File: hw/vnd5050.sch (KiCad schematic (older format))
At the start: 8 parts, among them U301 VND5050AJTR-E

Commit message: 050518: Kikepera head prototype first revision, saw not working
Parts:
- C301: symbol 4.7uF -> icu-rescue:4.7uF
- D301, D302, D303: symbol DIODE_RS07J-GS18 -> icu-rescue:DIODE_RS07J-GS18
- R301, R302: symbol 1K -> icu-rescue:1K
- R303: symbol 390 -> icu-rescue:390
- U301: symbol VND5050AJTR-E -> icu-rescue:VND5050AJTR-E
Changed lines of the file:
@@
-EESchema Schematic File Version 2
-LIBS:kemet
-LIBS:usevolt
-LIBS:wurth_elektronik_LED
-LIBS:power
-LIBS:yageo
+EESchema Schematic File Version 4
 LIBS:icu-cache
 EELAYER 26 0
@@
 SENSE
 $Comp
-L VND5050AJTR-E U301
+L icu-rescue:VND5050AJTR-E U301
 U 1 1 59D8088A
 P 4600 4000
@@
 AR Path="/5A7B577E/59D8088A" Ref="U801"  Part="1"
 AR Path="/5A7B753D/59D8088A" Ref="U901"  Part="1"
-F 0 "U301" H 4700 4447 60  0000 C CNN
+F 0 "U501" H 4700 4447 60  0000 C CNN
 F 1 "VND5050AJTR-E" H 4700 4341 60  0000 C CNN
 F 2 "usevolt:PowerSSO-12" H 4600 4400 60  0001 C CNN
@@
 $EndComp
 $Comp
-L VDD #PWR045
+L icu-rescue:VDD #PWR045
 U 1 1 59D808C7
 P 5250 3650
@@
 AR Path="/5A7B577E/59D808C7" Ref="#PWR029"  Part="1"
 AR Path="/5A7B753D/59D808C7" Ref="#PWR033"  Part="1"
-F 0 "#PWR045" H 5250 3500 50  0001 C CNN
+F 0 "#PWR017" H 5250 3500 50  0001 C CNN
 F 1 "VDD" H 5267 3823 50  0000 C CNN
 F 2 "" H 5250 3650 50  0000 C CNN
@@
 $EndComp
 $Comp
-L GND #PWR046
+L icu-rescue:GND #PWR046
 U 1 1 59D86DC2
 P 2950 4450
@@
 AR Path="/5A7B577E/59D86DC2" Ref="#PWR030"  Part="1"
 AR Path="/5A7B753D/59D86DC2" Ref="#PWR034"  Part="1"
-F 0 "#PWR046" H 2950 4200 50  0001 C CNN
+F 0 "#PWR018" H 2950 4200 50  0001 C CNN
 F 1 "GND" H 2955 4277 50  0000 C CNN
 F 2 "" H 2950 4450 50  0000 C CNN
@@
 $EndComp
 $Comp
-L 390 R?
+L icu-rescue:390 R?
 U 1 1 59D88845
 P 3150 3550
@@
 AR Path="/5A7B577E/59D88845" Ref="R803"  Part="1"
 AR Path="/5A7B753D/59D88845" Ref="R903"  Part="1"
-F 0 "R303" H 3200 3734 45  0000 C CNN
+F 0 "R503" H 3200 3734 45  0000 C CNN
 F 1 "390" H 3200 3650 45  0000 C CNN
 F 2 "yageo:0603" H 3180 3700 20  0001 C CNN
@@
 $EndComp
 $Comp
-L 1K R?
+L icu-rescue:1K R?
 U 1 1 5A05950C
 P 2750 3550
@@
 AR Path="/5A7B577E/5A05950C" Ref="R801"  Part="1"
 AR Path="/5A7B753D/5A05950C" Ref="R901"  Part="1"
-F 0 "R301" H 2800 3734 45  0000 C CNN
+F 0 "R501" H 2800 3734 45  0000 C CNN
 F 1 "1K" H 2800 3650 45  0000 C CNN
 F 2 "yageo:0603" H 2780 3700 20  0001 C CNN
@@
 $EndComp
 $Comp
-L 1K R?
+L icu-rescue:1K R?
 U 1 1 5A059568
 P 2750 4100
@@
 AR Path="/5A7B577E/5A059568" Ref="R802"  Part="1"
 AR Path="/5A7B753D/5A059568" Ref="R902"  Part="1"
-F 0 "R302" H 2800 4284 45  0000 C CNN
+F 0 "R502" H 2800 4284 45  0000 C CNN
 F 1 "1K" H 2800 4200 45  0000 C CNN
 F 2 "yageo:0603" H 2780 4250 20  0001 C CNN
@@
 $EndComp
 $Comp
-L DIODE_RS07J-GS18 D302
+L icu-rescue:DIODE_RS07J-GS18 D302
 U 1 1 5A2AAF9E
 P 5450 4750
@@
 AR Path="/5A7B577E/5A2AAF9E" Ref="D802"  Part="1"
 AR Path="/5A7B753D/5A2AAF9E" Ref="D902"  Part="1"
-F 0 "D302" V 5400 4652 45  0000 R CNN
+F 0 "D502" V 5400 4652 45  0000 R CNN
 F 1 "DIODE_RS07J-GS18" H 5470 4690 45  0001 L BNN
 F 2 "usevolt:DO219AB" H 5480 4900 20  0001 C CNN
@@
 $EndComp
 $Comp
-L DIODE_RS07J-GS18 D303
+L icu-rescue:DIODE_RS07J-GS18 D303
 U 1 1 5A2AB087
 P 5700 4750
@@
 AR Path="/5A7B577E/5A2AB087" Ref="D803"  Part="1"
 AR Path="/5A7B753D/5A2AB087" Ref="D903"  Part="1"
-F 0 "D303" V 5650 4652 45  0000 R CNN
+F 0 "D503" V 5650 4652 45  0000 R CNN
 F 1 "DIODE_RS07J-GS18" H 5720 4690 45  0001 L BNN
 F 2 "usevolt:DO219AB" H 5730 4900 20  0001 C CNN
@@
 $EndComp
 $Comp
-L GND #PWR047
+L icu-rescue:GND #PWR047
 U 1 1 5A2AB10F
 P 5550 5150
@@
 AR Path="/5A7B577E/5A2AB10F" Ref="#PWR031"  Part="1"
 AR Path="/5A7B753D/5A2AB10F" Ref="#PWR035"  Part="1"
-F 0 "#PWR047" H 5550 4900 50  0001 C CNN
+F 0 "#PWR019" H 5550 4900 50  0001 C CNN
 F 1 "GND" H 5555 4977 50  0000 C CNN
 F 2 "" H 5550 5150 50  0000 C CNN
@@
 $EndComp
 Wire Wire Line
-	5250 3650 5250 4000
+	5250 3650 5250 3800
 Wire Wire Line
 	5250 3800 5100 3800
@@
 Connection ~ 5250 3900
 Wire Wire Line
-	5100 4100 5800 4100
+	5100 4100 5250 4100
 Wire Wire Line
 	5100 4200 5250 4200
@@
 Connection ~ 5250 4100
 Wire Wire Line
-	5100 4400 5800 4400
+	5100 4400 5250 4400
 Wire Wire Line
 	5100 4300 5250 4300
@@
 Connection ~ 5250 4400
 Wire Wire Line
-	2550 3450 4300 3450
-Wire Wire Line
-	2550 4000 4300 4000
-Wire Wire Line
-	2950 3550 2950 4450
+	2550 3450 2650 3450
+Wire Wire Line
+	2550 4000 2650 4000
+Wire Wire Line
+	2950 3550 2950 4100
 Wire Wire Line
 	2950 4300 4300 4300
@@
 Connection ~ 2950 4100
 Wire Wire Line
-	3350 3550 4150 3550
-Wire Wire Line
-	3500 3200 3500 3550
+	3350 3550 3500 3550
+Wire Wire Line
+	3500 3200 3500 3350
 Wire Wire Line
 	3500 3350 2550 3350
@@
 	5700 5050 5700 4950
 Wire Wire Line
-	5450 5050 5700 5050
+	5450 5050 5550 5050
 Wire Wire Line
 	5450 5050 5450 4950
@@
 	4300 3900 4150 3900
 Wire Wire Line
-	4150 3550 4150 4100
+	4150 3550 4150 3900
 Wire Wire Line
 	4300 3450 4300 3800
 $Comp
-L 4.7uF C301
+L icu-rescue:4.7uF C301
 U 1 1 5A708309
 P 3150 3850
@@
 AR Path="/5A7B577E/5A708309" Ref="C801"  Part="1"
 AR Path="/5A7B753D/5A708309" Ref="C901"  Part="1"
-F 0 "C301" H 3200 4049 45  0000 C CNN
+F 0 "C501" H 3200 4049 45  0000 C CNN
 F 1 "4.7uF" H 3200 3965 45  0000 C CNN
 F 2 "kemet:0603" H 3180 4000 20  0001 C CNN
@@
 Connection ~ 4150 3900
 $Comp
-L DIODE_RS07J-GS18 D301
+L icu-rescue:DIODE_RS07J-GS18 D301
 U 1 1 5A7BC689
 P 3700 3200
@@
 AR Path="/5A7B577E/5A7BC689" Ref="D801"  Part="1"
 AR Path="/5A7B753D/5A7BC689" Ref="D901"  Part="1"
-F 0 "D301" H 3650 3340 45  0000 C CNN
+F 0 "D501" H 3650 3340 45  0000 C CNN
 F 1 "DIODE_RS07J-GS18" H 3720 3140 45  0001 L BNN
 F 2 "usevolt:DO219AB" H 3730 3350 20  0001 C CNN
@@
 Connection ~ 3500 3350
 $Comp
-L +3V3 #PWR048
+L icu-rescue:+3V3 #PWR048
 U 1 1 5A7BC750
 P 3900 3100
@@
 AR Path="/5A7B577E/5A7BC750" Ref="#PWR032"  Part="1"
 AR Path="/5A7B753D/5A7BC750" Ref="#PWR036"  Part="1"
-F 0 "#PWR048" H 3900 2950 50  0001 C CNN
+AR Path="/5A7BC750" Ref="#PWR048"  Part="1"
+F 0 "#PWR020" H 3900 2950 50  0001 C CNN
 F 1 "+3V3" H 3915 3273 50  0000 C CNN
 F 2 "" H 3900 3100 50  0000 C CNN
@@
 Wire Wire Line
 	3900 3200 3800 3200
+Wire Wire Line
+	5250 3800 5250 3900
+Wire Wire Line
+	5250 3900 5250 4000
+Wire Wire Line
+	5250 4100 5450 4100
+Wire Wire Line
+	5250 4400 5700 4400
+Wire Wire Line
+	2950 4300 2950 4450
+Wire Wire Line
+	2950 4100 2950 4300
+Wire Wire Line
+	3500 3550 4150 3550
+Wire Wire Line
+	2650 3450 4300 3450
+Wire Wire Line
+	2650 4000 4300 4000
+Wire Wire Line
+	5700 4400 5800 4400
+Wire Wire Line
+	5450 4100 5800 4100
+Wire Wire Line
+	5550 5050 5700 5050
+Wire Wire Line
+	4150 3900 4150 4100
+Wire Wire Line
+	3500 3350 3500 3550
 $EndSCHEMATC

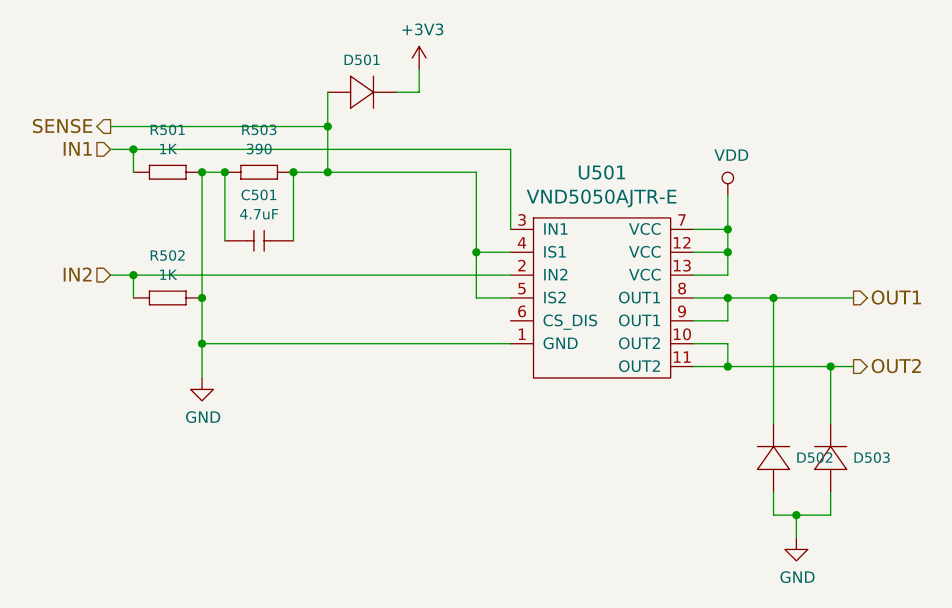
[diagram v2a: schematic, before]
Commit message: analog inputs replaced with digital inputs
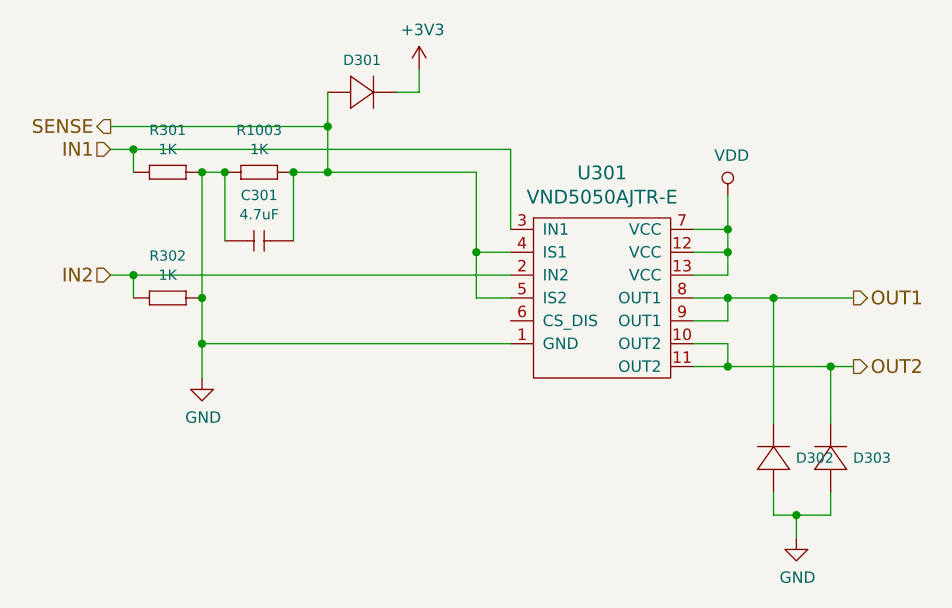
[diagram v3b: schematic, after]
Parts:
- removed R303: 390, yageo:0603, symbol icu-rescue:390
- added R603: 1K, yageo:0603, symbol yageo:1K
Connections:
- net GND: now also R603.2 (R2)
- net SENSE: now also R603.1 (R1)
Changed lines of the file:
@@
 $Descr A4 11693 8268
 encoding utf-8
-Sheet 4 14
+Sheet 6 10
 Title ""
 Date ""
@@
 AR Path="/5A7B577E/59D8088A" Ref="U801"  Part="1"
 AR Path="/5A7B753D/59D8088A" Ref="U901"  Part="1"
-F 0 "U501" H 4700 4447 60  0000 C CNN
+F 0 "U301" H 4700 4447 60  0000 C CNN
 F 1 "VND5050AJTR-E" H 4700 4341 60  0000 C CNN
 F 2 "usevolt:PowerSSO-12" H 4600 4400 60  0001 C CNN
@@
 AR Path="/5A7B577E/59D808C7" Ref="#PWR029"  Part="1"
 AR Path="/5A7B753D/59D808C7" Ref="#PWR033"  Part="1"
-F 0 "#PWR017" H 5250 3500 50  0001 C CNN
+F 0 "#PWR045" H 5250 3500 50  0001 C CNN
 F 1 "VDD" H 5267 3823 50  0000 C CNN
 F 2 "" H 5250 3650 50  0000 C CNN
@@
 AR Path="/5A7B577E/59D86DC2" Ref="#PWR030"  Part="1"
 AR Path="/5A7B753D/59D86DC2" Ref="#PWR034"  Part="1"
-F 0 "#PWR018" H 2950 4200 50  0001 C CNN
+F 0 "#PWR046" H 2950 4200 50  0001 C CNN
 F 1 "GND" H 2955 4277 50  0000 C CNN
 F 2 "" H 2950 4450 50  0000 C CNN
 F 3 "" H 2950 4450 50  0000 C CNN
 	1    2950 4450
-	1    0    0    -1
-$EndComp
-$Comp
-L icu-rescue:390 R?
-U 1 1 59D88845
-P 3150 3550
-AR Path="/5A015FC0/59D88845" Ref="R?"  Part="1"
-AR Path="/5A02A41F/59D88845" Ref="R?"  Part="1"
-AR Path="/5A12B58E/59D88845" Ref="R?"  Part="1"
-AR Path="/5A7B157A/59D88845" Ref="R303"  Part="1"
-AR Path="/5A7B341B/59D88845" Ref="R503"  Part="1"
-AR Path="/5A7B2C1B/59D88845" Ref="R403"  Part="1"
-AR Path="/5A7B3FAD/59D88845" Ref="R603"  Part="1"
-AR Path="/5A7B4C13/59D88845" Ref="R703"  Part="1"
-AR Path="/5A7B577E/59D88845" Ref="R803"  Part="1"
-AR Path="/5A7B753D/59D88845" Ref="R903"  Part="1"
-F 0 "R503" H 3200 3734 45  0000 C CNN
-F 1 "390" H 3200 3650 45  0000 C CNN
-F 2 "yageo:0603" H 3180 3700 20  0001 C CNN
-F 3 "" H 3119 3589 60  0001 C CNN
-F 4 "" H 3519 3989 60  0001 C CNN "1st Source Part Number"
-F 5 "Digikey" H 3419 3889 60  0001 C CNN "1st Source"
-F 6 "RC0603FR-07390RL" H 3319 3789 60  0001 C CNN "Manufacturer Part Number"
-F 7 "YAGEO" H 3219 3689 60  0001 C CNN "Manufacturer"
-	1    3150 3550
 	1    0    0    -1
 $EndComp
@@
 AR Path="/5A7B577E/5A05950C" Ref="R801"  Part="1"
 AR Path="/5A7B753D/5A05950C" Ref="R901"  Part="1"
-F 0 "R501" H 2800 3734 45  0000 C CNN
+F 0 "R301" H 2800 3734 45  0000 C CNN
 F 1 "1K" H 2800 3650 45  0000 C CNN
 F 2 "yageo:0603" H 2780 3700 20  0001 C CNN
@@
 AR Path="/5A7B577E/5A059568" Ref="R802"  Part="1"
 AR Path="/5A7B753D/5A059568" Ref="R902"  Part="1"
-F 0 "R502" H 2800 4284 45  0000 C CNN
+F 0 "R302" H 2800 4284 45  0000 C CNN
 F 1 "1K" H 2800 4200 45  0000 C CNN
 F 2 "yageo:0603" H 2780 4250 20  0001 C CNN
@@
 AR Path="/5A7B577E/5A2AAF9E" Ref="D802"  Part="1"
 AR Path="/5A7B753D/5A2AAF9E" Ref="D902"  Part="1"
-F 0 "D502" V 5400 4652 45  0000 R CNN
+F 0 "D302" V 5400 4652 45  0000 R CNN
 F 1 "DIODE_RS07J-GS18" H 5470 4690 45  0001 L BNN
 F 2 "usevolt:DO219AB" H 5480 4900 20  0001 C CNN
@@
 AR Path="/5A7B577E/5A2AB087" Ref="D803"  Part="1"
 AR Path="/5A7B753D/5A2AB087" Ref="D903"  Part="1"
-F 0 "D503" V 5650 4652 45  0000 R CNN
+F 0 "D303" V 5650 4652 45  0000 R CNN
 F 1 "DIODE_RS07J-GS18" H 5720 4690 45  0001 L BNN
 F 2 "usevolt:DO219AB" H 5730 4900 20  0001 C CNN
@@
 AR Path="/5A7B577E/5A2AB10F" Ref="#PWR031"  Part="1"
 AR Path="/5A7B753D/5A2AB10F" Ref="#PWR035"  Part="1"
-F 0 "#PWR019" H 5550 4900 50  0001 C CNN
+F 0 "#PWR047" H 5550 4900 50  0001 C CNN
 F 1 "GND" H 5555 4977 50  0000 C CNN
 F 2 "" H 5550 5150 50  0000 C CNN
@@
 AR Path="/5A7B577E/5A708309" Ref="C801"  Part="1"
 AR Path="/5A7B753D/5A708309" Ref="C901"  Part="1"
-F 0 "C501" H 3200 4049 45  0000 C CNN
+F 0 "C301" H 3200 4049 45  0000 C CNN
 F 1 "4.7uF" H 3200 3965 45  0000 C CNN
 F 2 "kemet:0603" H 3180 4000 20  0001 C CNN
@@
 Wire Wire Line
 	3050 3850 3050 3550
-Connection ~ 3050 3550
 Wire Wire Line
 	3350 3850 3350 3550
-Connection ~ 3350 3550
 Wire Wire Line
 	4150 4100 4300 4100
@@
 AR Path="/5A7B577E/5A7BC689" Ref="D801"  Part="1"
 AR Path="/5A7B753D/5A7BC689" Ref="D901"  Part="1"
-F 0 "D501" H 3650 3340 45  0000 C CNN
+F 0 "D301" H 3650 3340 45  0000 C CNN
 F 1 "DIODE_RS07J-GS18" H 3720 3140 45  0001 L BNN
 F 2 "usevolt:DO219AB" H 3730 3350 20  0001 C CNN
@@
 AR Path="/5A7B753D/5A7BC750" Ref="#PWR036"  Part="1"
 AR Path="/5A7BC750" Ref="#PWR048"  Part="1"
-F 0 "#PWR020" H 3900 2950 50  0001 C CNN
+F 0 "#PWR048" H 3900 2950 50  0001 C CNN
 F 1 "+3V3" H 3915 3273 50  0000 C CNN
 F 2 "" H 3900 3100 50  0000 C CNN
@@
 Wire Wire Line
 	3500 3350 3500 3550
+$Comp
+L yageo:1K R603
+U 1 1 5B1E176A
+P 3150 3550
+AR Path="/5A7B4C13/5B1E176A" Ref="R603"  Part="1"
+AR Path="/5A7B2C1B/5B1E176A" Ref="R303"  Part="1"
+AR Path="/5A7B341B/5B1E176A" Ref="R403"  Part="1"
+AR Path="/5A7B3FAD/5B1E176A" Ref="R503"  Part="1"
+AR Path="/5A7B577E/5B1E176A" Ref="R703"  Part="1"
+AR Path="/5A7B753D/5B1E176A" Ref="R803"  Part="1"
+AR Path="/5A7B157A/5B1E176A" Ref="R1003"  Part="1"
+F 0 "R1003" H 3200 3734 45  0000 C CNN
+F 1 "1K" H 3200 3650 45  0000 C CNN
+F 2 "yageo:0603" H 3180 3700 20  0001 C CNN
+F 3 "" H 3119 3589 60  0001 C CNN
+F 4 "" H 3519 3989 60  0001 C CNN "1st Source Part Number"
+F 5 "Digikey" H 3419 3889 60  0001 C CNN "1st Source"
+F 6 "RC0603FR-071KL" H 3319 3789 60  0001 C CNN "Manufacturer Part Number"
+F 7 "YAGEO" H 3219 3689 60  0001 C CNN "Manufacturer"
+	1    3150 3550
+	1    0    0    -1
+$EndComp
+Connection ~ 3350 3550
+Connection ~ 3050 3550
 $EndSCHEMATC

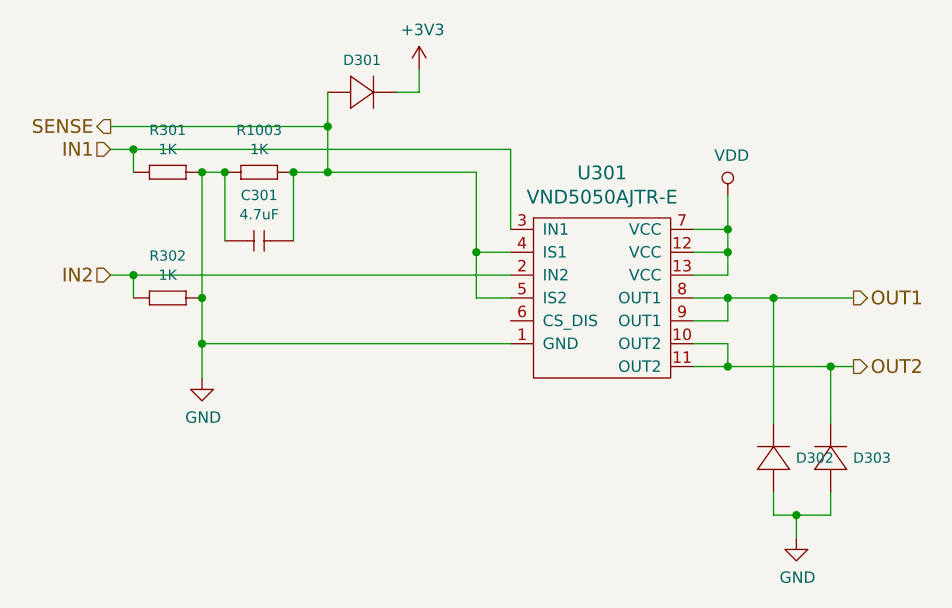
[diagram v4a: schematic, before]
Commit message: 2 din replaced with ain, zeners added to outputs
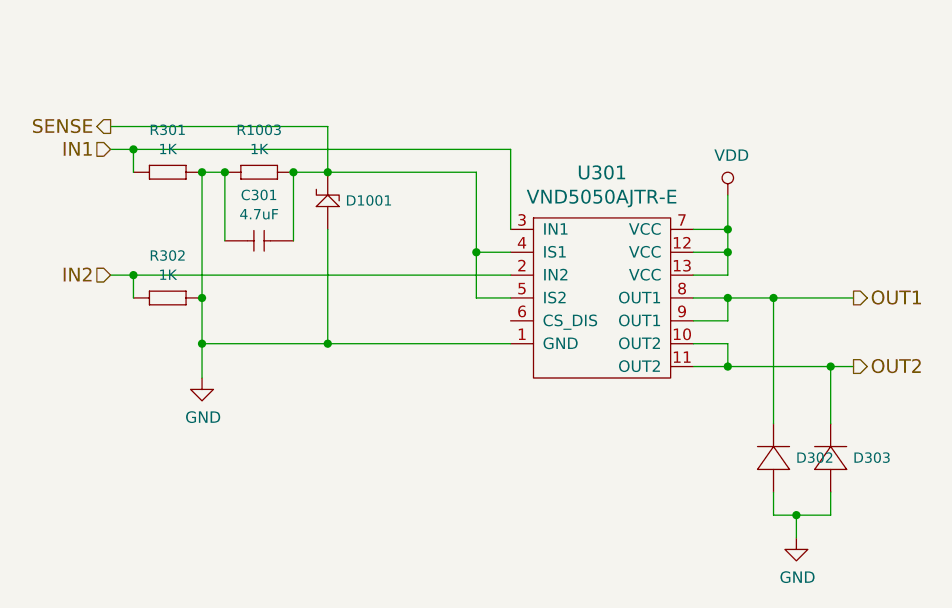
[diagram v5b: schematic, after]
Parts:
- removed D301: DIODE_RS07J-GS18, usevolt:DO219AB, symbol icu-rescue:DIODE_RS07J-GS18
- added D801: ZENER_MM3Z3V6T1G, usevolt:SOD-323, symbol usevolt:ZENER_MM3Z3V6T1G
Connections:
- net GND: now also D801.2
- net SENSE: now also D801.1
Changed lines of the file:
@@
 $Descr A4 11693 8268
 encoding utf-8
-Sheet 6 11
+Sheet 8 13
 Title ""
 Date ""
@@
 	2950 3550 2950 4100
 Wire Wire Line
-	2950 4300 4300 4300
+	2950 4300 3500 4300
 Wire Wire Line
 	3050 3550 2950 3550
@@
 Wire Wire Line
 	3350 3550 3500 3550
-Wire Wire Line
-	3500 3200 3500 3350
 Wire Wire Line
 	3500 3350 2550 3350
@@
 	4150 4100 4300 4100
 Connection ~ 4150 3900
-$Comp
-L icu-rescue:DIODE_RS07J-GS18 D301
-U 1 1 5A7BC689
-P 3700 3200
-AR Path="/5A7B157A/5A7BC689" Ref="D301"  Part="1"
-AR Path="/5A7B341B/5A7BC689" Ref="D501"  Part="1"
-AR Path="/5A7B2C1B/5A7BC689" Ref="D401"  Part="1"
-AR Path="/5A7B3FAD/5A7BC689" Ref="D601"  Part="1"
-AR Path="/5A7B4C13/5A7BC689" Ref="D701"  Part="1"
-AR Path="/5A7B577E/5A7BC689" Ref="D801"  Part="1"
-AR Path="/5A7B753D/5A7BC689" Ref="D901"  Part="1"
-F 0 "D301" H 3650 3340 45  0000 C CNN
-F 1 "DIODE_RS07J-GS18" H 3720 3140 45  0001 L BNN
-F 2 "usevolt:DO219AB" H 3730 3350 20  0001 C CNN
-F 3 "http://www.vishay.com/docs/85742/rs07b.pdf" H 3720 3220 60  0001 C CNN
-F 4 "1864882" H 4320 3820 60  0001 C CNN "2nd Source Part Number"
-F 5 "Digi-Key" H 4020 3520 60  0001 C CNN "1st Source"
-F 6 "Farnell" H 4220 3720 60  0001 C CNN "2nd Source"
-F 7 "RS07J-GS18" H 3920 3420 60  0001 C CNN "Manufacturer Part Number"
-F 8 "RS07J-GS18-ND" H 4120 3620 60  0001 C CNN "1st Source Part Number"
-F 9 "Vishay Semiconductor Diodes Division" H 3820 3320 60  0001 C CNN "Manufacturer"
-	1    3700 3200
-	1    0    0    -1
-$EndComp
-Connection ~ 3500 3350
-$Comp
-L icu-rescue:+3V3 #PWR048
-U 1 1 5A7BC750
-P 3900 3100
-AR Path="/5A7B157A/5A7BC750" Ref="#PWR048"  Part="1"
-AR Path="/5A7B341B/5A7BC750" Ref="#PWR020"  Part="1"
-AR Path="/5A7B2C1B/5A7BC750" Ref="#PWR016"  Part="1"
-AR Path="/5A7B3FAD/5A7BC750" Ref="#PWR024"  Part="1"
-AR Path="/5A7B4C13/5A7BC750" Ref="#PWR028"  Part="1"
-AR Path="/5A7B577E/5A7BC750" Ref="#PWR032"  Part="1"
-AR Path="/5A7B753D/5A7BC750" Ref="#PWR036"  Part="1"
-AR Path="/5A7BC750" Ref="#PWR048"  Part="1"
-F 0 "#PWR048" H 3900 2950 50  0001 C CNN
-F 1 "+3V3" H 3915 3273 50  0000 C CNN
-F 2 "" H 3900 3100 50  0000 C CNN
-F 3 "" H 3900 3100 50  0000 C CNN
-	1    3900 3100
-	1    0    0    -1
-$EndComp
-Wire Wire Line
-	3900 3100 3900 3200
-Wire Wire Line
-	3900 3200 3800 3200
 Wire Wire Line
 	5250 3800 5250 3900
@@
 Connection ~ 3350 3550
 Connection ~ 3050 3550
+$Comp
+L usevolt:ZENER_MM3Z3V6T1G D801
+U 1 1 5B753167
+P 3500 3600
+AR Path="/5A7B753D/5B753167" Ref="D801"  Part="1"
+AR Path="/5A7B2C1B/5B753167" Ref="D301"  Part="1"
+AR Path="/5A7B341B/5B753167" Ref="D401"  Part="1"
+AR Path="/5A7B3FAD/5B753167" Ref="D501"  Part="1"
+AR Path="/5A7B4C13/5B753167" Ref="D601"  Part="1"
+AR Path="/5A7B577E/5B753167" Ref="D701"  Part="1"
+AR Path="/5A7B157A/5B753167" Ref="D1001"  Part="1"
+F 0 "D1001" V 3425 3522 45  0000 R CNN
+F 1 "ZENER_MM3Z3V6T1G" H 3775 3975 45  0001 L BNN
+F 2 "usevolt:SOD-323" H 3475 3975 20  0001 C CNN
+F 3 "http://www.mouser.com/ds/2/308/MM3Z2V4T1-D-269162.pdf" H 3850 4175 60  0001 C CNN
+F 4 "Mouser" H 3820 3920 60  0001 C CNN "1st Source"
+F 5 "MM3Z3V6T1G" H 3720 3820 60  0001 C CNN "Manufacturer Part Number"
+F 6 "863-MM3Z3V6T1G" H 3920 4020 60  0001 C CNN "1st Source Part Number"
+F 7 "ON Semiconductor" H 3775 4075 60  0001 C CNN "Manufacturer"
+	1    3500 3600
+	0    -1   -1   0
+$EndComp
+Wire Wire Line
+	3500 3800 3500 4300
+Connection ~ 3500 4300
+Wire Wire Line
+	3500 4300 4300 4300
 $EndSCHEMATC
